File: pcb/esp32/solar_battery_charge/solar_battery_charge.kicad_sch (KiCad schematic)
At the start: 12 parts, among them J1 USB_A, J2 Conn_01x02_Female, J3 Conn_01x02_Female, J4 Screw_Terminal_01x02, J5 Conn_01x02_Female, J6 Conn_01x02_Female, J7 Conn_01x01_Male, J8 Conn_01x01_Male, U1 LM7805_TO220, U2 MCP1700-1202E_TO92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

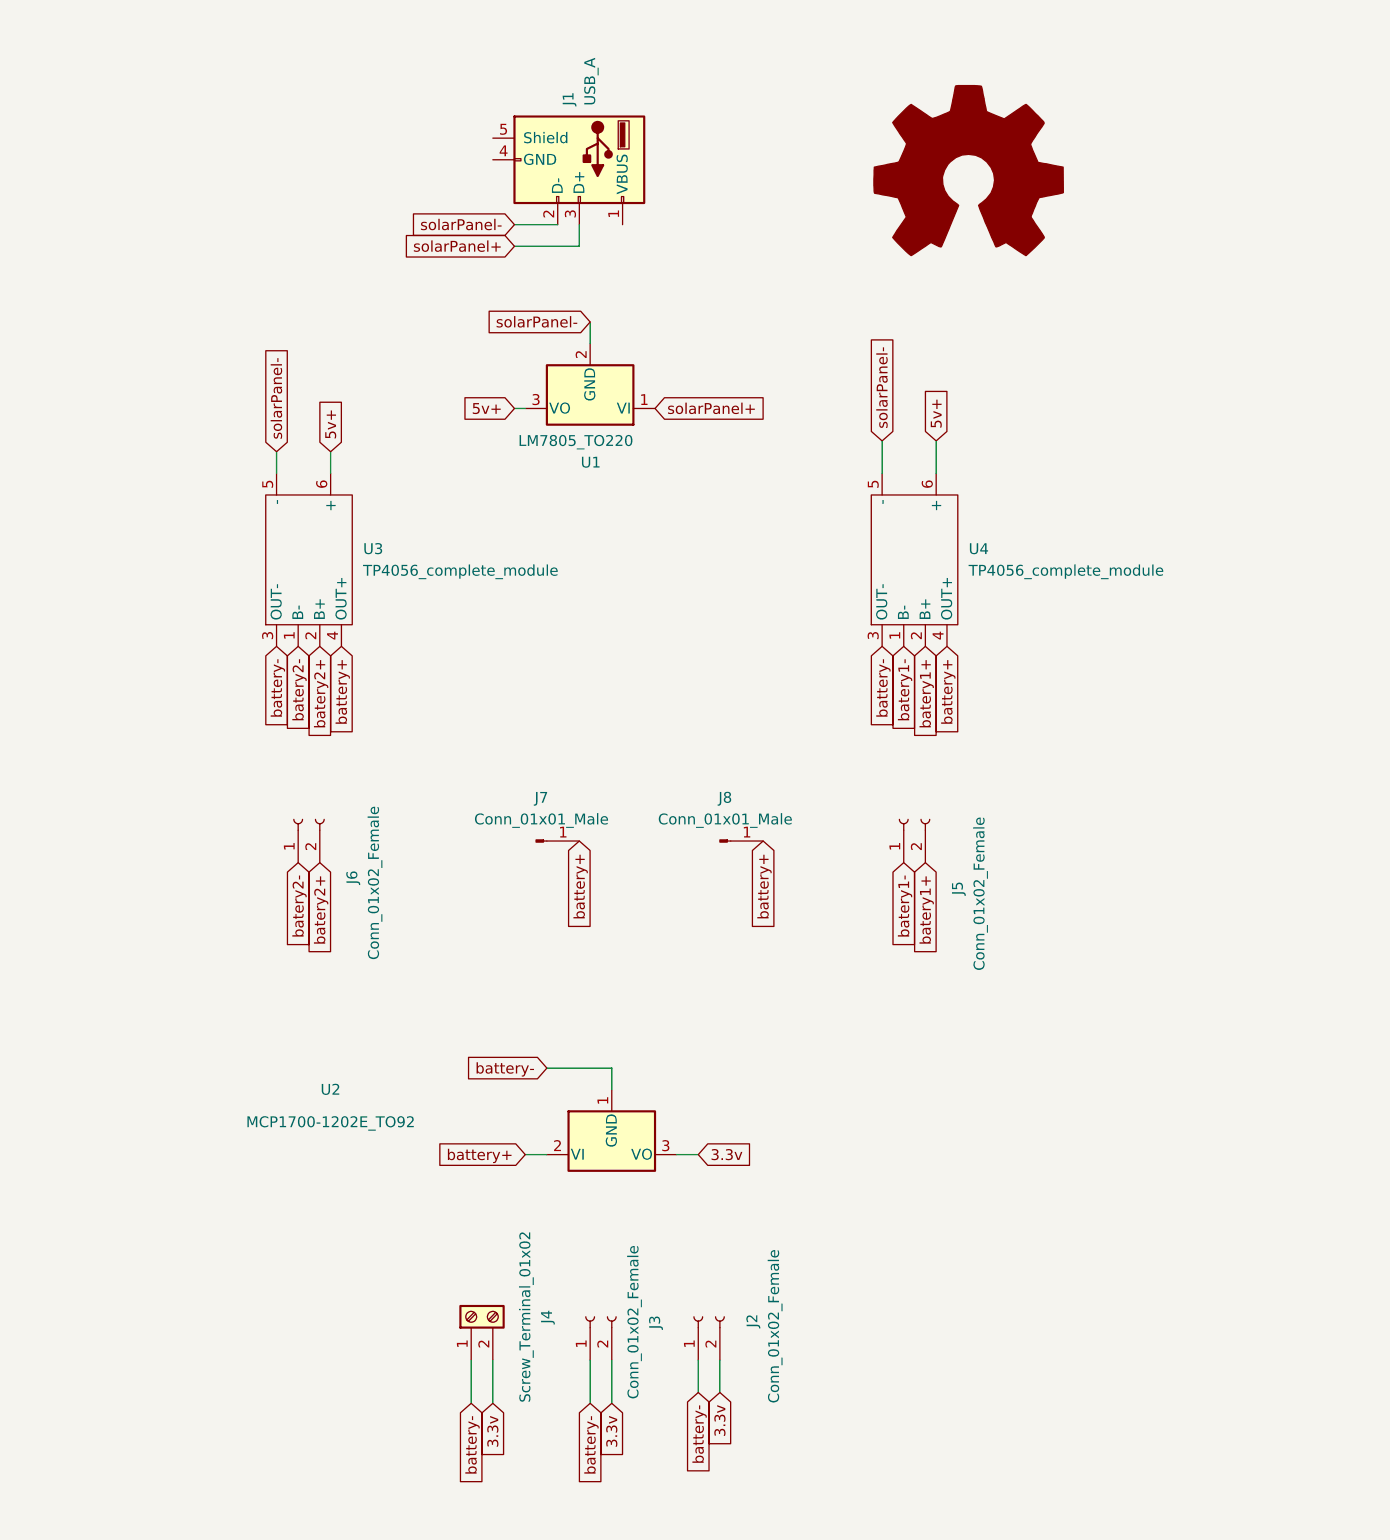
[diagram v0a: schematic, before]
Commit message: updated solar baterry charge pcb, by changing lm7805 for ams1117 voltage regulator, also repositioned the layout
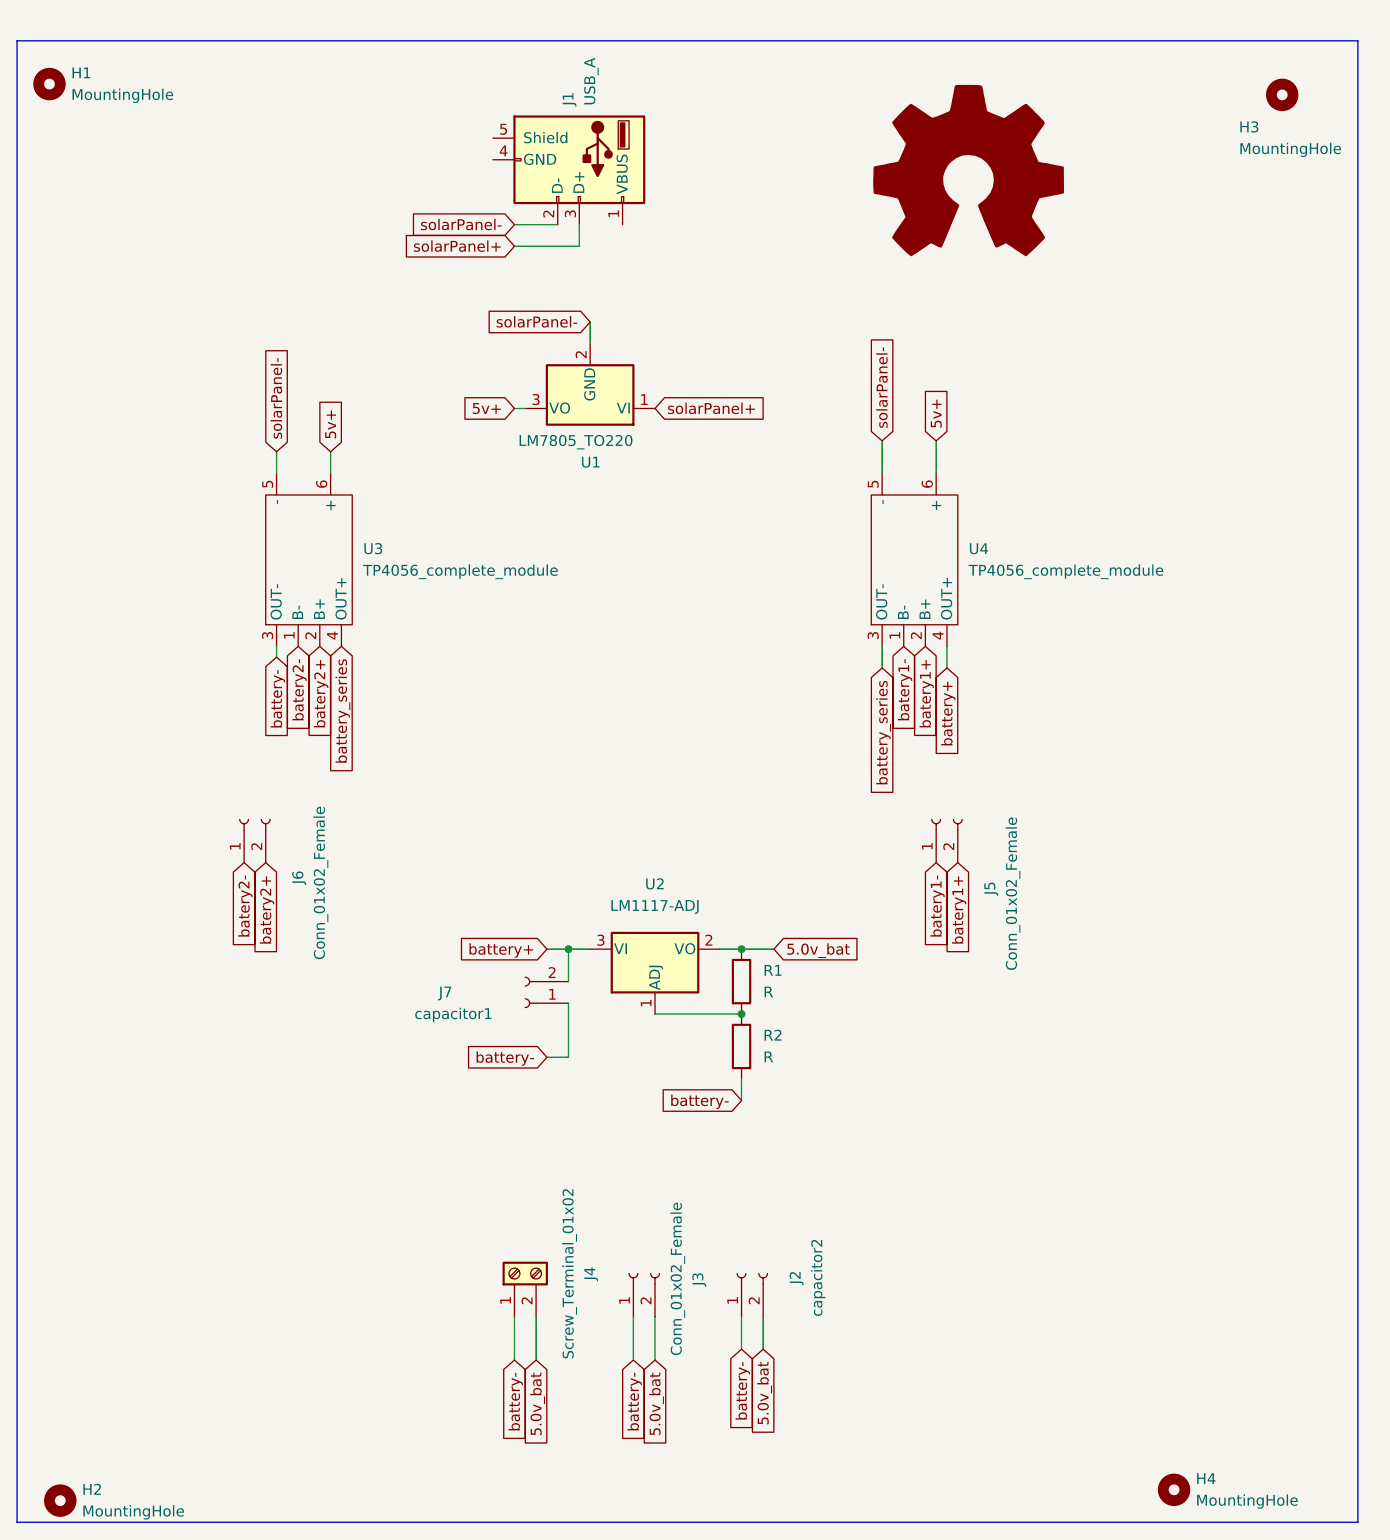
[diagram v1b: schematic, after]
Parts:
- removed J7: Conn_01x01_Male, symbol Connector:Conn_01x01_Male
- removed J8: Conn_01x01_Male, Connector_PinHeader_2.00mm:PinHeader_1x01_P2.00mm_Vertical, symbol Connector:Conn_01x01_Male
- removed U2: MCP1700-1202E_TO92, smart_sensor:Connector_Molex__Molex_SL_171971-0003_1x03_P2.54mm_Vertical, symbol Regulator_Linear:MCP1700-1202E_TO92
- added H1: MountingHole, symbol Mechanical:MountingHole
- added H2, H3, H4: MountingHole, MountingHole:MountingHole_2mm, symbol Mechanical:MountingHole
- added J7: capacitor1, smart_sensor:Connector_Molex_Molex_SL_171971-0004_1x02_P2.54mm_Vertical_squares, symbol Connector:Conn_01x02_Female
- added R1, R2: R, Resistor_THT:R_Axial_DIN0204_L3.6mm_D1.6mm_P5.08mm_Horizontal, symbol Device:R
- added U2: LM1117-ADJ, Package_TO_SOT_SMD:SOT-223-3_TabPin2, symbol Regulator_Linear:LM1117-ADJ
- J2: value Conn_01x02_Female -> capacitor2
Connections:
- net battery+: now also J7.2 (Pin_2), U2.3 (VI); no longer U3.4 (OUT+)
- net battery-: now also J7.1 (Pin_1), R2.2; no longer U4.3 (OUT-)
- net 3.3v renamed 5.0v_bat
- net 5.0v_bat: now also R1.1, U2.2 (VO)
- new net: R1.2, R2.1, U2.1 (ADJ)
- new net battery_series: U3.4 (OUT+), U4.3 (OUT-)
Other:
- moved on the sheet: J2, J3, J4, J5, J6

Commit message: added diode to esp32 board and updated solar board to fixed 5.0v ams1117
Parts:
- removed R1, R2: R, Resistor_THT:R_Axial_DIN0204_L3.6mm_D1.6mm_P5.08mm_Horizontal, symbol Device:R
- removed U2: LM1117-ADJ, Package_TO_SOT_SMD:SOT-223-3_TabPin2, symbol Regulator_Linear:LM1117-ADJ
- added U2: LM1117-5.0, symbol Regulator_Linear:LM1117-5.0
- H1: footprint (none) -> MountingHole:MountingHole_2mm
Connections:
- net 5.0v_bat: now also U2.2 (VO)
- net battery+: now also U2.3 (VI)
- net battery-: now also U2.1 (GND)
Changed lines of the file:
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@@
   (junction (at 80.01 121.92) (diameter 0) (color 0 0 0 0)
   )
-  (junction (at 100.33 121.92) (diameter 0) (color 0 0 0 0)
-  )
-  (junction (at 100.33 129.54) (diameter 0) (color 0 0 0 0)
-  )
   (wire (pts (xy 124.46 88.9) (xy 124.46 86.36))
     (stroke (width 0) (type default) (color 0 0 0 0))
@@
     (stroke (width 0) (type default) (color 0 0 0 0))
   )
-  (wire (pts (xy 100.33 121.92) (xy 97.79 121.92))
-    (stroke (width 0) (type default) (color 0 0 0 0))
-  )
-  (wire (pts (xy 90.17 129.54) (xy 100.33 129.54))
+  (wire (pts (xy 97.79 121.92) (xy 104.14 121.92))
     (stroke (width 0) (type default) (color 0 0 0 0))
   )
@@
     (stroke (width 0) (type default) (color 0 0 0 0))
   )
-  (wire (pts (xy 100.33 139.7) (xy 100.33 137.16))
-    (stroke (width 0) (type default) (color 0 0 0 0))
-  )
   (wire (pts (xy 80.01 121.92) (xy 80.01 125.73))
     (stroke (width 0) (type default) (color 0 0 0 0))
@@
     (stroke (width 0) (type default) (color 0 0 0 0))
   )
-  (wire (pts (xy 104.14 121.92) (xy 100.33 121.92))
-    (stroke (width 0) (type default) (color 0 0 0 0))
-  )
   (wire (pts (xy 90.17 165.1) (xy 90.17 170.18))
     (stroke (width 0) (type default) (color 0 0 0 0))
@@
     (stroke (width 0) (type default) (color 0 0 0 0))
   )
+  (wire (pts (xy 90.17 129.54) (xy 90.17 134.62))
+    (stroke (width 0) (type default) (color 0 0 0 0))
+  )
   (wire (pts (xy 82.55 48.26) (xy 82.55 50.8))
     (stroke (width 0) (type default) (color 0 0 0 0))
@@
     )
   )
-  (global_label "battery-" (shape input) (at 100.33 139.7 180) (fields_autoplaced)
-    (effects (font (size 1.27 1.27)) (justify right))
-    (property "Intersheet References" "${INTERSHEET_REFS}" (id 0) (at 89.7526 139.7794 0)
-      (effects (font (size 1.27 1.27)) (justify right) hide)
+  (global_label "battery-" (shape input) (at 90.17 134.62 0) (fields_autoplaced)
+    (effects (font (size 1.27 1.27)) (justify left))
+    (property "Intersheet References" "${INTERSHEET_REFS}" (id 0) (at 100.7474 134.5406 0)
+      (effects (font (size 1.27 1.27)) (justify left) hide)
     )
   )
@@
     )
   )
-  (symbol (lib_id "Device:R") (at 100.33 133.35 0) (unit 1)
-    (in_bom yes) (on_board yes) (fields_autoplaced)
-    (property "Reference" "R2" (id 0) (at 102.87 132.0799 0)
-      (effects (font (size 1.27 1.27)) (justify left))
-    )
-    (property "Value" "R" (id 1) (at 102.87 134.6199 0)
-      (effects (font (size 1.27 1.27)) (justify left))
-    )
-    (property "Footprint" "Resistor_THT:R_Axial_DIN0204_L3.6mm_D1.6mm_P5.08mm_Horizontal" (id 2) (at 98.552 133.35 90)
-      (effects (font (size 1.27 1.27)) hide)
-    )
-    (property "Datasheet" "~" (id 3) (at 100.33 133.35 0)
-      (effects (font (size 1.27 1.27)) hide)
-    )
-    (pin "1")
-    (pin "2")
-  )
   (symbol (lib_id "Mechanical:MountingHole") (at 20.32 186.69 0) (unit 1)
     (in_bom yes) (on_board yes) (fields_autoplaced)
@@
       (effects (font (size 1.27 1.27)) hide)
     )
-  )
-  (symbol (lib_id "Device:R") (at 100.33 125.73 0) (unit 1)
-    (in_bom yes) (on_board yes) (fields_autoplaced)
-    (property "Reference" "R1" (id 0) (at 102.87 124.4599 0)
-      (effects (font (size 1.27 1.27)) (justify left))
-    )
-    (property "Value" "R" (id 1) (at 102.87 126.9999 0)
-      (effects (font (size 1.27 1.27)) (justify left))
-    )
-    (property "Footprint" "Resistor_THT:R_Axial_DIN0204_L3.6mm_D1.6mm_P5.08mm_Horizontal" (id 2) (at 98.552 125.73 90)
-      (effects (font (size 1.27 1.27)) hide)
-    )
-    (property "Datasheet" "~" (id 3) (at 100.33 125.73 0)
-      (effects (font (size 1.27 1.27)) hide)
-    )
-    (pin "1")
-    (pin "2")
   )
   (symbol (lib_id "Connector:Conn_01x02_Female") (at 87.63 160.02 90) (unit 1)
@@
       (effects (font (size 1.27 1.27)) (justify left))
     )
-    (property "Footprint" "" (id 2) (at 19.05 20.32 0)
+    (property "Footprint" "MountingHole:MountingHole_2mm" (id 2) (at 19.05 20.32 0)
       (effects (font (size 1.27 1.27)) hide)
     )
@@
     (pin "5")
   )
-  (symbol (lib_id "Regulator_Linear:LM1117-ADJ") (at 90.17 121.92 0) (unit 1)
-    (in_bom yes) (on_board yes) (fields_autoplaced)
-    (property "Reference" "U2" (id 0) (at 90.17 114.3 0))
-    (property "Value" "LM1117-ADJ" (id 1) (at 90.17 116.84 0))
-    (property "Footprint" "Package_TO_SOT_SMD:SOT-223-3_TabPin2" (id 2) (at 90.17 121.92 0)
-      (effects (font (size 1.27 1.27)) hide)
-    )
-    (property "Datasheet" "http://www.ti.com/lit/ds/symlink/lm1117.pdf" (id 3) (at 90.17 121.92 0)
-      (effects (font (size 1.27 1.27)) hide)
-    )
-    (pin "1")
-    (pin "2")
-    (pin "3")
-  )
   (symbol (lib_id "Connector:Screw_Terminal_01x02") (at 73.66 160.02 90) (unit 1)
     (in_bom yes) (on_board yes) (fields_autoplaced)
@@
     )
     (property "Datasheet" "https://www.onsemi.cn/PowerSolutions/document/MC7800-D.PDF" (id 3) (at 82.55 57.15 0)
+      (effects (font (size 1.27 1.27)) hide)
+    )
+    (pin "1")
+    (pin "2")
+    (pin "3")
+  )
+  (symbol (lib_id "Regulator_Linear:LM1117-5.0") (at 90.17 121.92 0) (unit 1)
+    (in_bom yes) (on_board yes) (fields_autoplaced)
+    (property "Reference" "U2" (id 0) (at 90.17 114.3 0))
+    (property "Value" "LM1117-5.0" (id 1) (at 90.17 116.84 0))
+    (property "Footprint" "" (id 2) (at 90.17 121.92 0)
+      (effects (font (size 1.27 1.27)) hide)
+    )
+    (property "Datasheet" "http://www.ti.com/lit/ds/symlink/lm1117.pdf" (id 3) (at 90.17 121.92 0)
       (effects (font (size 1.27 1.27)) hide)
     )
@@
       (reference "J7") (unit 1) (value "capacitor1") (footprint "smart_sensor:Connector_Molex_Molex_SL_171971-0004_1x02_P2.54mm_Vertical_squares")
     )
-    (path "/75d56fe8-9064-410b-af6a-6f6da3648af7"
-      (reference "R1") (unit 1) (value "R") (footprint "Resistor_THT:R_Axial_DIN0204_L3.6mm_D1.6mm_P5.08mm_Horizontal")
-    )
-    (path "/4eb5eb8d-3dce-4ab5-b051-2b3b2c19d2a3"
-      (reference "R2") (unit 1) (value "R") (footprint "Resistor_THT:R_Axial_DIN0204_L3.6mm_D1.6mm_P5.08mm_Horizontal")
-    )
     (path "/c36a9a9a-1d9e-4ab6-a67f-0c9f31ad7ce6"
       (reference "U1") (unit 1) (value "LM7805_TO220") (footprint "smart_sensor:Package_TO_SOT_THT__TO-220-3_Vertical_solar_charger")
     )
-    (path "/9cf513cc-5582-4e42-9bdf-16d5625f3ab1"
-      (reference "U2") (unit 1) (value "LM1117-ADJ") (footprint "Package_TO_SOT_SMD:SOT-223-3_TabPin2")
+    (path "/d1e79c7b-1c3a-478b-9075-1d456a8d3f1a"
+      (reference "U2") (unit 1) (value "LM1117-5.0") (footprint "Package_TO_SOT_SMD:SOT-223-3_TabPin2")
     )
     (path "/e59e8a86-c187-493e-97ea-b12a673ac232"
